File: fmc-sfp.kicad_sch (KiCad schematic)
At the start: 34 parts, among them J1 ASP-134604-01, J2 SFP+, J3 SFP+, J4 132134, J5 132134, J6 132134, J7 132134, SW1 CHS-02TB, U1 MAX9113EKA_TT, U2 MAX9113EKA_TT

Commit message: clean up schematic and pcb
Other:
- moved on the sheet: R1, R11, R12, R13, R14, R2, R3, R4, R5, R6, SW1

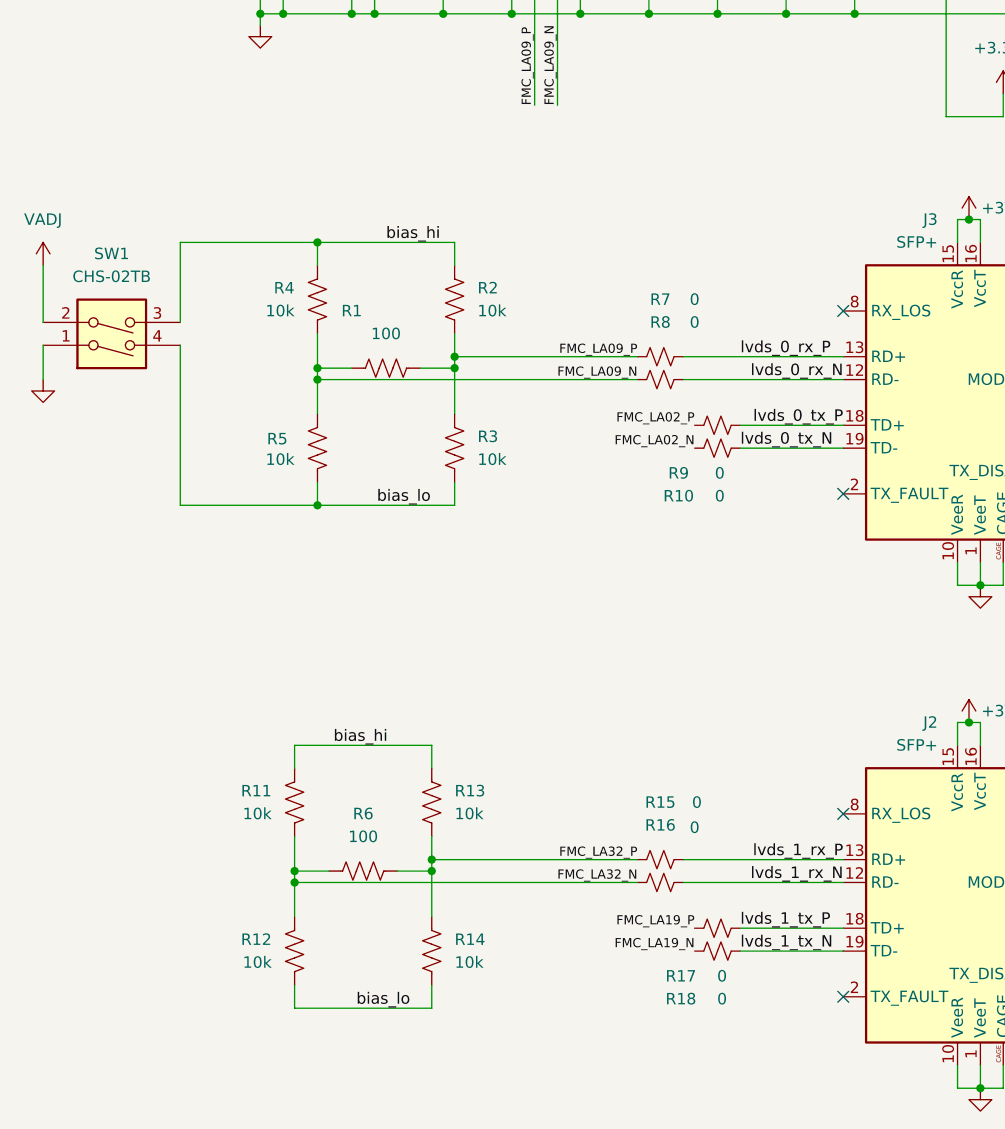
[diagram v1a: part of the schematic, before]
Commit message: make board more symetrical
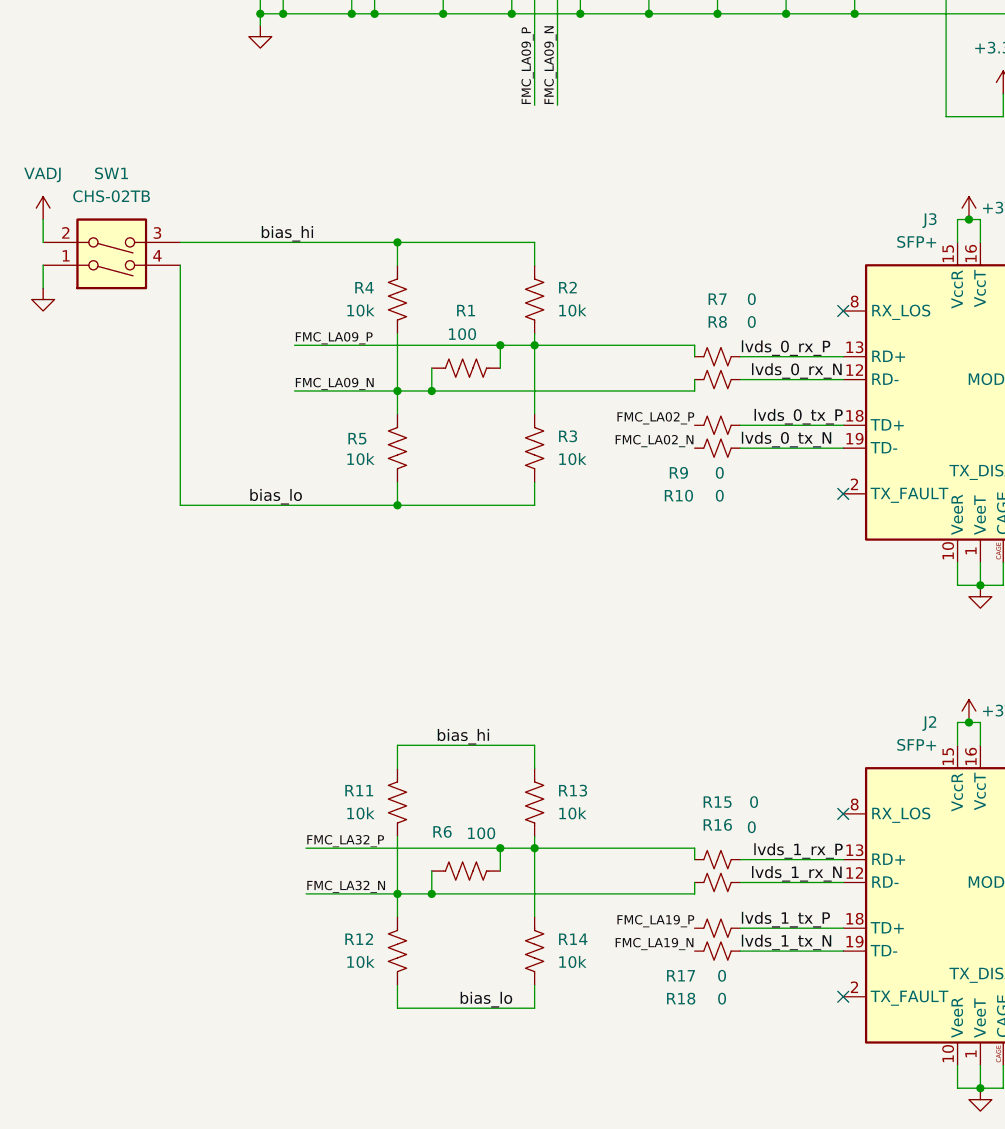
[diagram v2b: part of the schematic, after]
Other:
- moved on the sheet: R1, R11, R12, R13, R14, R15, R16, R2, R3, R4, R5, R6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

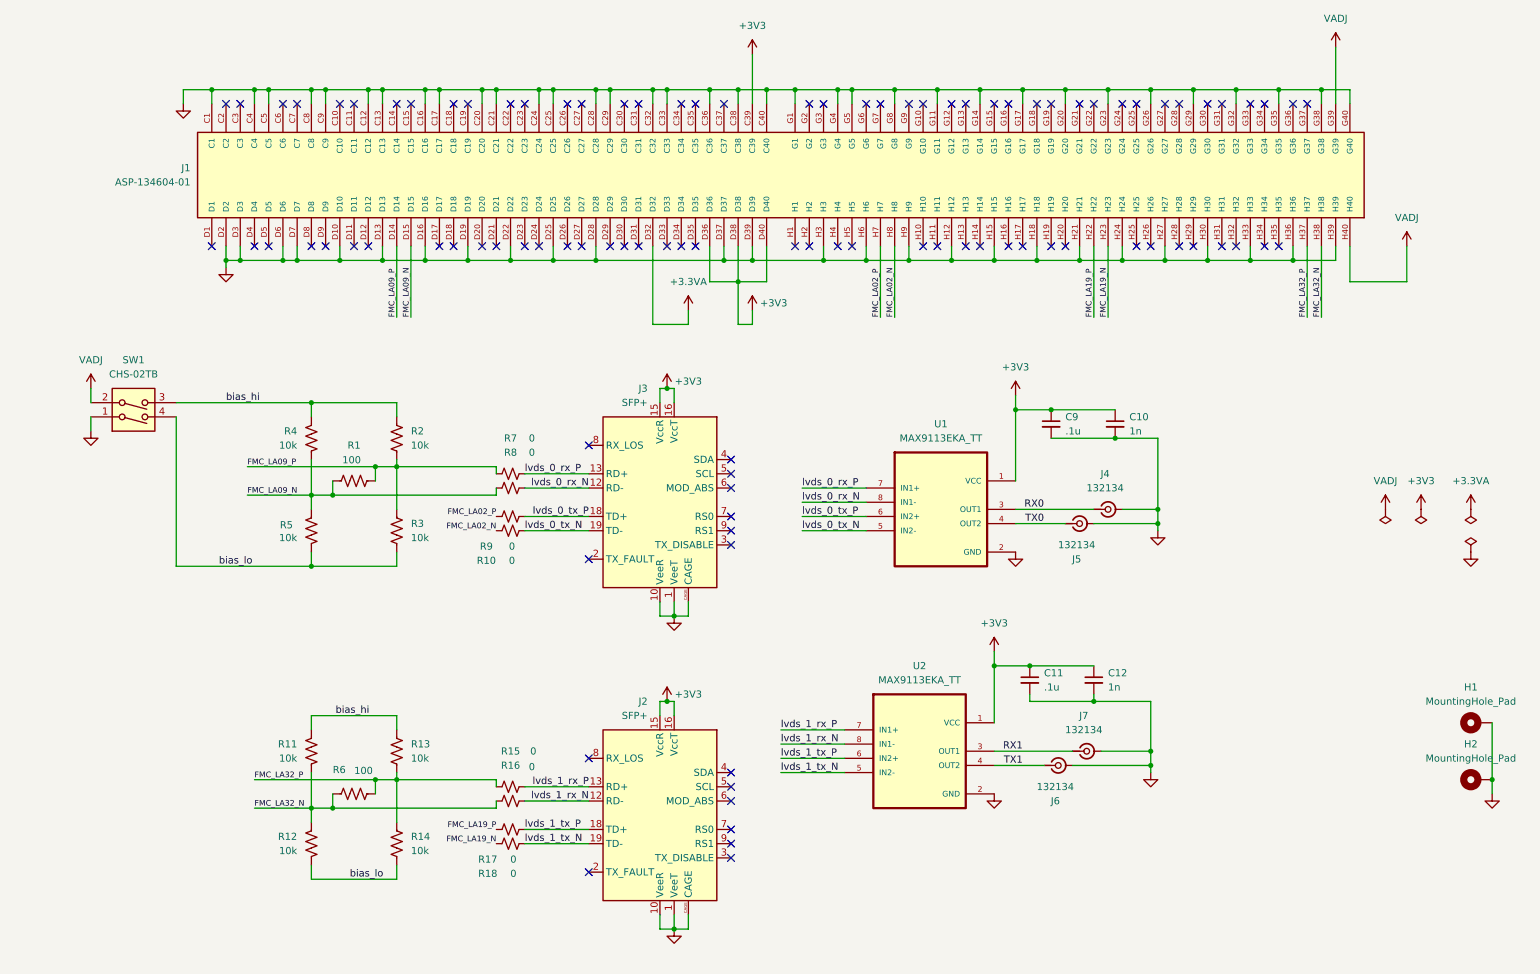
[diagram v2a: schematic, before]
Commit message: add single x4 switch and test pads for differential probing
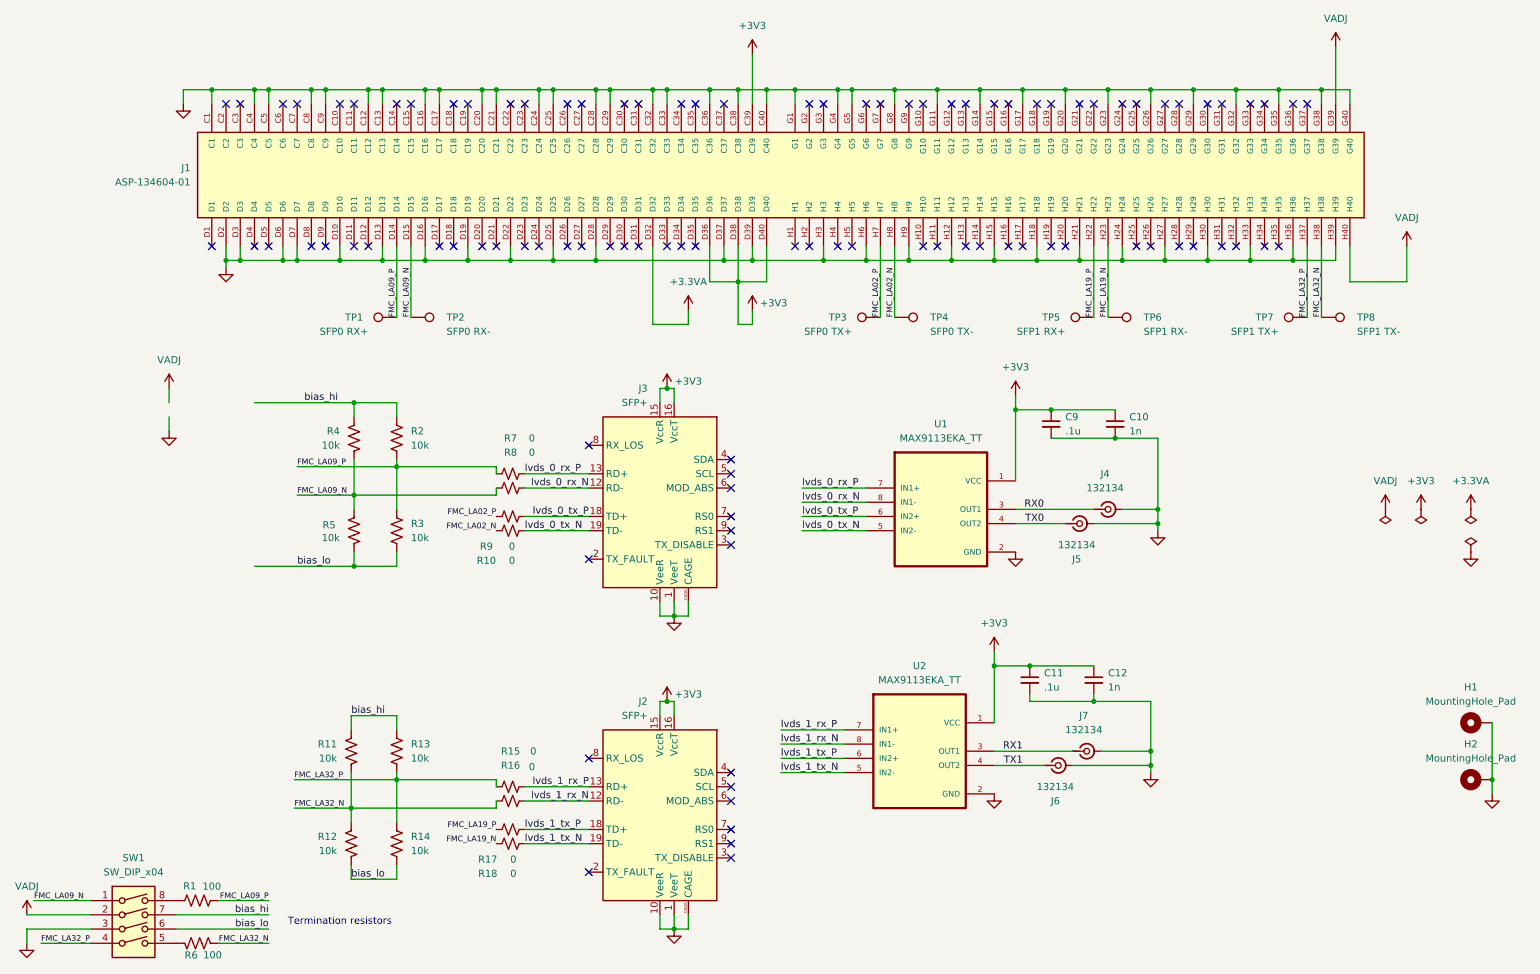
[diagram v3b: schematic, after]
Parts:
- removed SW1: CHS-02TB, Button_Switch_SMD:SW_DIP_SPSTx02_Slide_Copal_CHS-02B_W7.62mm_P1.27mm, symbol Switch:SW_DIP_x02
- added SW1: SW_DIP_x04, Button_Switch_SMD:SW_DIP_SPSTx04_Slide_Copal_CHS-04A_W5.08mm_P1.27mm_JPin, symbol Switch:SW_DIP_x04
- added TP1: SFP0 RX+, TestPoint:TestPoint_Pad_D4.0mm, symbol Connector:TestPoint
- added TP2: SFP0 RX-, TestPoint:TestPoint_Pad_D4.0mm, symbol Connector:TestPoint
- added TP3: SFP0 TX+, TestPoint:TestPoint_Pad_D4.0mm, symbol Connector:TestPoint
- added TP4: SFP0 TX-, TestPoint:TestPoint_Pad_D4.0mm, symbol Connector:TestPoint
- added TP5: SFP1 RX+, TestPoint:TestPoint_Pad_D4.0mm, symbol Connector:TestPoint
- added TP6: SFP1 RX-, TestPoint:TestPoint_Pad_D4.0mm, symbol Connector:TestPoint
- added TP7: SFP1 TX+, TestPoint:TestPoint_Pad_D4.0mm, symbol Connector:TestPoint
- added TP8: SFP1 TX-, TestPoint:TestPoint_Pad_D4.0mm, symbol Connector:TestPoint
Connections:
- net FMC_LA02_N: now also TP4.1
- net FMC_LA02_P: now also TP3.1
- net FMC_LA09_N: now also SW1.1, TP2.1; no longer R1.1
- net FMC_LA09_P: now also TP1.1
- net FMC_LA19_N: now also TP6.1
- net FMC_LA19_P: now also TP5.1
- net FMC_LA32_N: now also R6.2, TP8.1; no longer R6.1
- net FMC_LA32_P: now also SW1.4, TP7.1; no longer R6.2
- net GND: now also SW1.3
- net VADJ: now also SW1.2
- net bias_hi: now also SW1.7
- net bias_lo: now also SW1.6
- new net: R1.1, SW1.8
- new net: R6.1, SW1.5
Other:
- note added: "Termination resistors"
- moved on the sheet: R1, R11, R12, R4, R5, R6

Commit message: cleanup schematic
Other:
- note added: "Termination resistors and bias voltage"
- note removed: "Termination resistors"
- moved on the sheet: R1, R11, R12, R6, SW1

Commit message: exclude test points from BOM
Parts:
- TP1, TP2, TP3, TP4, TP5, TP6, TP7, TP8: now left out of the parts list
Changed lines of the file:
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@@
 		(title "FMC-SFP")
 		(date "2024-06-11")
-		(rev "Rev1")
+		(rev "Rev0a-16-g620039f-dirty")
 		(company "MicroRidge Technology LTD")
 	)
@@
 		(unit 1)
 		(exclude_from_sim no)
-		(in_bom yes)
+		(in_bom no)
 		(on_board yes)
 		(dnp no)
@@
 		(unit 1)
 		(exclude_from_sim no)
-		(in_bom yes)
+		(in_bom no)
 		(on_board yes)
 		(dnp no)
@@
 		(unit 1)
 		(exclude_from_sim no)
-		(in_bom yes)
+		(in_bom no)
 		(on_board yes)
 		(dnp no)
@@
 		(unit 1)
 		(exclude_from_sim no)
-		(in_bom yes)
+		(in_bom no)
 		(on_board yes)
 		(dnp no)
@@
 		(unit 1)
 		(exclude_from_sim no)
-		(in_bom yes)
+		(in_bom no)
 		(on_board yes)
 		(dnp no)
@@
 		(unit 1)
 		(exclude_from_sim no)
-		(in_bom yes)
+		(in_bom no)
 		(on_board yes)
 		(dnp no)
@@
 		(unit 1)
 		(exclude_from_sim no)
-		(in_bom yes)
+		(in_bom no)
 		(on_board yes)
 		(dnp no)
@@
 		(unit 1)
 		(exclude_from_sim no)
-		(in_bom yes)
+		(in_bom no)
 		(on_board yes)
 		(dnp no)

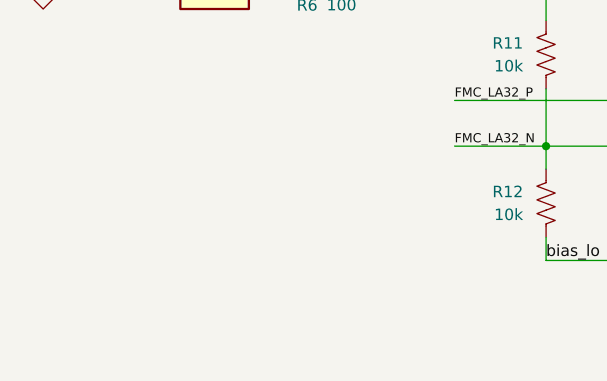
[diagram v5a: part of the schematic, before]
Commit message: asthetic cleanup, add ground testpoint
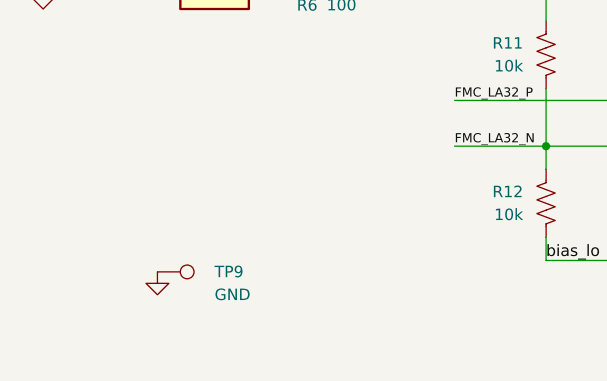
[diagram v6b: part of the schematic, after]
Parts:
- added TP9: GND, TestPoint:TestPoint_Keystone_5015_Micro-Minature, symbol Connector:TestPoint
- TP1, TP2, TP3, TP4, TP5, TP6, TP7, TP8: footprint TestPoint:TestPoint_Pad_D4.0mm -> TestPoint:TestPoint_Pad_D2.5mm
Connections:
- net GND: now also TP9.1
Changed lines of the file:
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@@
 			)
 		)
-		(property "Footprint" "TestPoint:TestPoint_Pad_D4.0mm"
+		(property "Footprint" "TestPoint:TestPoint_Pad_D2.5mm"
 			(at 246.38 69.85 0)
 			(effects
@@
 			)
 		)
-		(property "Footprint" "TestPoint:TestPoint_Pad_D4.0mm"
+		(property "Footprint" "TestPoint:TestPoint_Pad_D2.5mm"
 			(at 172.72 80.01 0)
 			(effects
@@
 	)
 	(symbol
+		(lib_id "Connector:TestPoint")
+		(at 31.75 176.53 270)
+		(unit 1)
+		(exclude_from_sim no)
+		(in_bom yes)
+		(on_board yes)
+		(dnp no)
+		(property "Reference" "TP9"
+			(at 38.1 176.53 90)
+			(effects
+				(font
+					(size 1.27 1.27)
+				)
+				(justify left)
+			)
+		)
+		(property "Value" "GND"
+			(at 38.1 179.07 90)
+			(effects
+				(font
+					(size 1.27 1.27)
+				)
+				(justify left)
+			)
+		)
+		(property "Footprint" "TestPoint:TestPoint_Keystone_5015_Micro-Minature"
+			(at 31.75 181.61 0)
+			(effects
+				(font
+					(size 1.27 1.27)
+				)
+				(hide yes)
+			)
+		)
+		(property "Datasheet" "~"
+			(at 31.75 181.61 0)
+			(effects
+				(font
+					(size 1.27 1.27)
+				)
+				(hide yes)
+			)
+		)
+		(property "Description" "test point"
+			(at 31.75 176.53 0)
+			(effects
+				(font
+					(size 1.27 1.27)
+				)
+				(hide yes)
+			)
+		)
+		(property "MANUFACTURER" "Keystone Electronics"
+			(at 31.75 176.53 0)
+			(effects
+				(font
+					(size 1.27 1.27)
+				)
+				(hide yes)
+			)
+		)
+		(property "MPN" "5015"
+			(at 31.75 176.53 0)
+			(effects
+				(font
+					(size 1.27 1.27)
+				)
+				(hide yes)
+			)
+		)
+		(pin "1"
+		)
+		(instances
+			(project "fmc-sfp"
+				(path "/9a4127e9-981d-42fd-bc3c-a0fb85e0287b"
+					(reference "TP9")
+					(unit 1)
+				)
+			)
+		)
+	)
+	(symbol
 		(lib_id "power:PWR_FLAG")
 		(at 275.59 109.22 180)
@@
 	)
 	(symbol
+		(lib_id "power:GND")
+		(at 31.75 176.53 0)
+		(unit 1)
+		(exclude_from_sim no)
+		(in_bom yes)
+		(on_board yes)
+		(dnp no)
+		(fields_autoplaced yes)
+		(property "Reference" "#PWR06"
+			(at 31.75 182.88 0)
+			(effects
+				(font
+					(size 1.27 1.27)
+				)
+				(hide yes)
+			)
+		)
+		(property "Value" "GND"
+			(at 31.75 181.61 0)
+			(effects
+				(font
+					(size 1.27 1.27)
+				)
+				(hide yes)
+			)
+		)
+		(property "Footprint" ""
+			(at 31.75 176.53 0)
+			(effects
+				(font
+					(size 1.27 1.27)
+				)
+				(hide yes)
+			)
+		)
+		(property "Datasheet" ""
+			(at 31.75 176.53 0)
+			(effects
+				(font
+					(size 1.27 1.27)
+				)
+				(hide yes)
+			)
+		)
+		(property "Description" "Power symbol creates a global label with name \"GND\" , ground"
+			(at 31.75 176.53 0)
+			(effects
+				(font
+					(size 1.27 1.27)
+				)
+				(hide yes)
+			)
+		)
+		(pin "1"
+		)
+		(instances
+			(project "fmc-sfp"
+				(path "/9a4127e9-981d-42fd-bc3c-a0fb85e0287b"
+					(reference "#PWR06")
+					(unit 1)
+				)
+			)
+		)
+	)
+	(symbol
 		(lib_id "Device:R_Small_US")
 		(at 104.14 102.87 90)
@@
 			)
 		)
-		(property "Footprint" "TestPoint:TestPoint_Pad_D4.0mm"
+		(property "Footprint" "TestPoint:TestPoint_Pad_D2.5mm"
 			(at 83.82 69.85 0)
 			(effects
@@
 			)
 		)
-		(property "Footprint" "TestPoint:TestPoint_Pad_D4.0mm"
+		(property "Footprint" "TestPoint:TestPoint_Pad_D2.5mm"
 			(at 248.92 80.01 0)
 			(effects
@@
 			)
 		)
-		(property "Footprint" "TestPoint:TestPoint_Pad_D4.0mm"
+		(property "Footprint" "TestPoint:TestPoint_Pad_D2.5mm"
 			(at 210.82 80.01 0)
 			(effects
@@
 			)
 		)
-		(property "Footprint" "TestPoint:TestPoint_Pad_D4.0mm"
+		(property "Footprint" "TestPoint:TestPoint_Pad_D2.5mm"
 			(at 86.36 80.01 0)
 			(effects
@@
 			)
 		)
-		(property "Footprint" "TestPoint:TestPoint_Pad_D4.0mm"
+		(property "Footprint" "TestPoint:TestPoint_Pad_D2.5mm"
 			(at 208.28 69.85 0)
 			(effects
@@
 			)
 		)
-		(property "Footprint" "TestPoint:TestPoint_Pad_D4.0mm"
+		(property "Footprint" "TestPoint:TestPoint_Pad_D2.5mm"
 			(at 170.18 69.85 0)
 			(effects

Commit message: set SW1 part number
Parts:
- SW1: footprint Button_Switch_SMD:SW_DIP_SPSTx04_Slide_Copal_CHS-04A_W5.08mm_P1.27mm_JPin -> Button_Switch_SMD:SW_DIP_SPSTx04_Slide_KingTek_DSHP04TS_W7.62mm_P1.27mm; MANUFACTURER (none) -> DongGuan KINGTEK Industrial Co.,LTD; MPN (none) -> DongGuan KINGTEK Industrial Co.,LTD
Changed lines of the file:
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@@
 			)
 		)
-		(property "Footprint" "Button_Switch_SMD:SW_DIP_SPSTx04_Slide_Copal_CHS-04A_W5.08mm_P1.27mm_JPin"
+		(property "Footprint" "Button_Switch_SMD:SW_DIP_SPSTx04_Slide_KingTek_DSHP04TS_W7.62mm_P1.27mm"
 			(at 38.1 142.24 0)
 			(effects
@@
 			(at 38.1 142.24 0)
 			(effects
+				(font
+					(size 1.27 1.27)
+				)
+				(hide yes)
+			)
+		)
+		(property "MANUFACTURER" "DongGuan KINGTEK Industrial Co.,LTD "
+			(at 38.1 142.24 0)
+			(effects
+				(font
+					(size 1.27 1.27)
+				)
+				(hide yes)
+			)
+		)
+		(property "MPN" "DongGuan KINGTEK Industrial Co.,LTD "
+			(at 38.1 142.24 0)
+			(effects

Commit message: Update layout with i2c
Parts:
- removed C10, C12: 1n, Capacitor_SMD:C_0603_1608Metric, symbol Device:C_Small
- removed C11, C9: .1u, Capacitor_SMD:C_0603_1608Metric, symbol Device:C_Small
- removed J2, J3: SFP+, project:SFP_and_Cage, symbol Interface_Optical:SFP+
- removed J4, J5, J6, J7: 132134, Connector_Coaxial:SMA_Amphenol_132134_Vertical, symbol Connector:Conn_Coaxial_Small
- removed R10, R15, R16, R17, R18, R7, R8, R9: 0, Resistor_SMD:R_0805_2012Metric_Pad1.20x1.40mm_HandSolder, symbol Device:R_Small_US
- removed R11, R12, R13, R14, R2, R3, R4, R5: 10k, Resistor_SMD:R_0805_2012Metric_Pad1.20x1.40mm_HandSolder, symbol Device:R_US
- removed U1, U2: MAX9113EKA_TT, Package_TO_SOT_SMD:SOT-23-8, symbol project:MAX9113EKA_TT
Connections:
- net SFP1_TX_DISABLE: now reaches J1.D24
- net SFP1_RS1: now reaches J1.D26
- net SFP1_RS0: now reaches J1.D27
- net SFP1_MODABS: now reaches J1.D29
- net SFP1_SCL: now reaches J1.D30
- net SFP1_SDA: now reaches J1.D31
- net SFP0_TX_DISABLE: now reaches J1.H11
- net SFP0_RS1: now reaches J1.H13
- net SFP0_RS0: now reaches J1.H14
- net SFP0_MODABS: now reaches J1.H17
- net SFP0_SCL: now reaches J1.H19
- net SFP0_SDA: now reaches J1.H20
- no-connect marks 100 -> 72
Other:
- added sheet SFP0 (SFP.kicad_sch)
- added sheet SFP1 (SFP.kicad_sch)
